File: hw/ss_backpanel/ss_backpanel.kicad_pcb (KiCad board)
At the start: 2 copper layers, 165 x 51.1 mm, 16 parts, among them J101 4mm_banana_socket-LB_I4R_A-pa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, M101 Amphenol_T3437000-DIN7_panel_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, M102 Amphenol_T3437000-DIN7_panel_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, M103 Schurter-3101_0060-fuse_holde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, M104 FN283-1-06_Schaffner_AC-panel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, M105 74980104400-Wurth_RJ45-Panel_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, M106 TE-1734346-Panel_cutout, M107 CUI-UJ2_AH_1_SMT-Panel_cutout, M108 DSub9-Kycon_K22X-E9P-N-panel_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, M109 SJ-3571N_CUI_audio_jacket_pan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

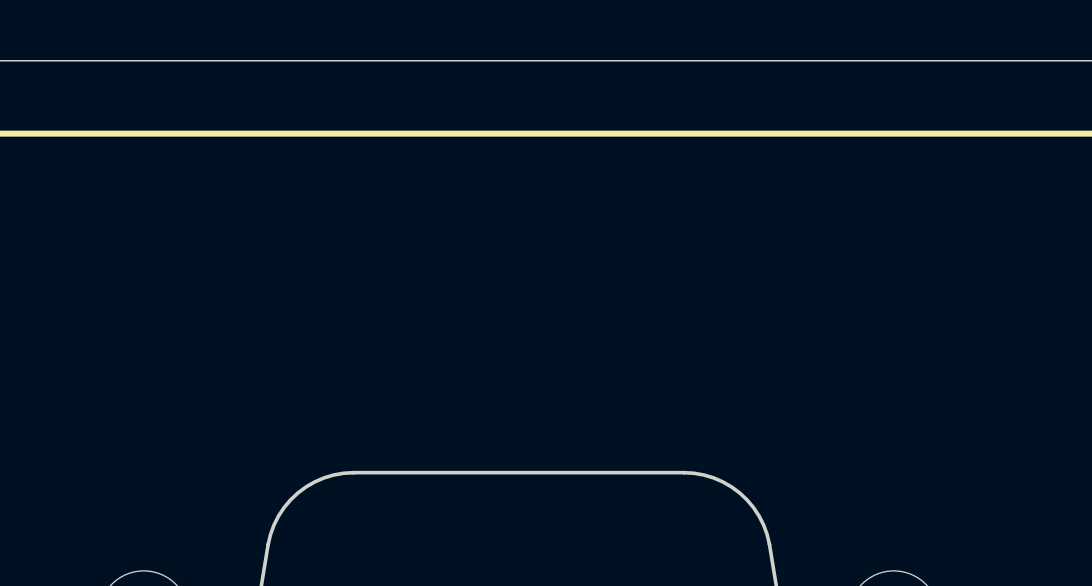
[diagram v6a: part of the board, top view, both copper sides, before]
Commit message: Add 12V DC-out (Molex Nano-Fit 1x02) and SMA in back-panel, for FM antenna & ext. ant.amp. Updated Dsub9 conn to correct component & placement on MB.
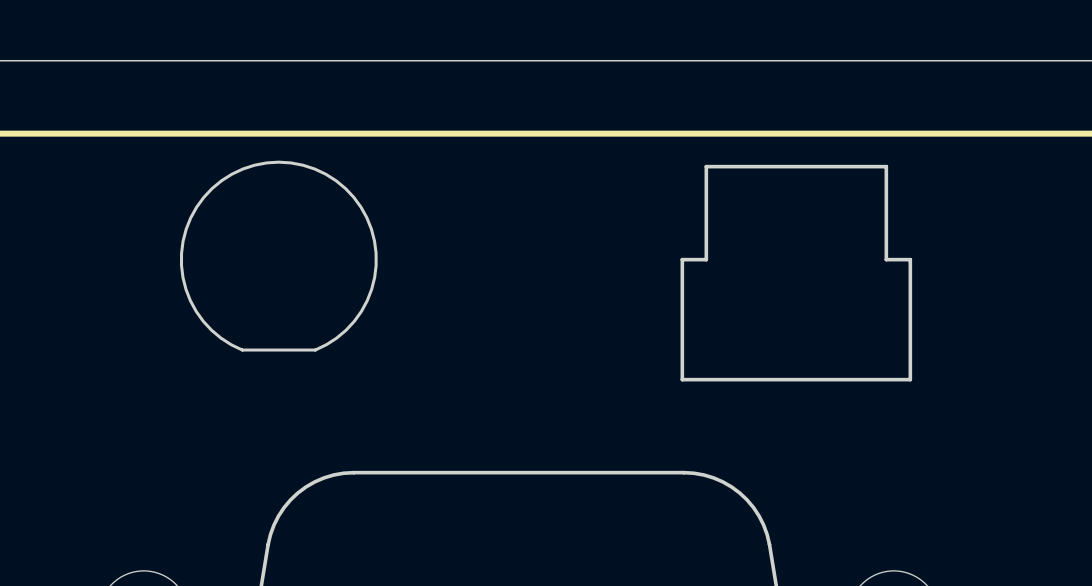
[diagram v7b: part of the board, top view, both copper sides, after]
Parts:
- added M110: SMA_bulkhead_jack_Panel_cutout, customlib_mj_fp:SMA_Bulkhead_jack-Panel_cutout, B.Cu at (95.5, 55.5)
- added M111: Molex_NanoFit-1x02-Panel_cutout, customlib_mj_fp:Molex_NanoFit-1x02-Panel_cutout, B.Cu at (112.8, 59.5)

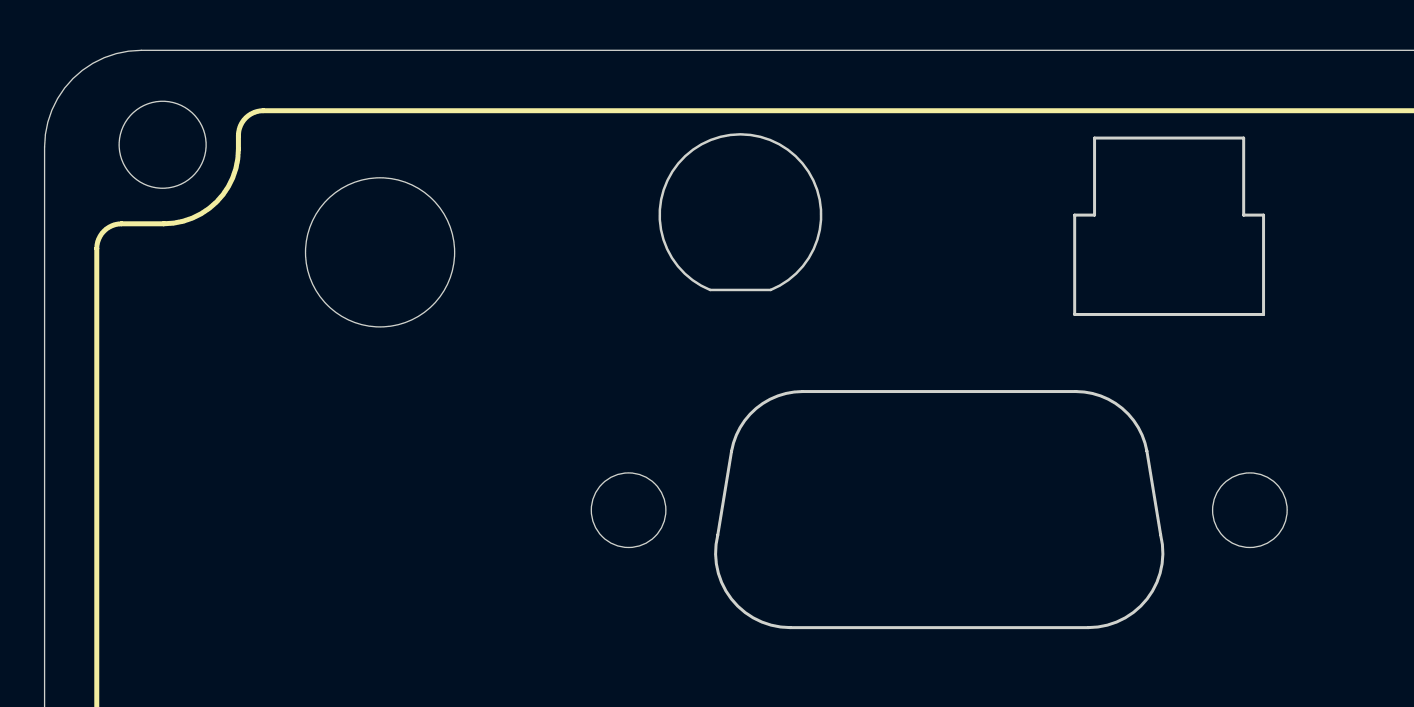
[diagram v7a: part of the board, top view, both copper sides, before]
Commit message: Backpanel: move SMA to side, under MB PCB, also 12V-out moved outwards (and had to shift 12V/Gnd pins);   Mainboard: Move SMA-RA to bottomside, wont fit on Topside. ALso prelim. scatter/placement of some comps.
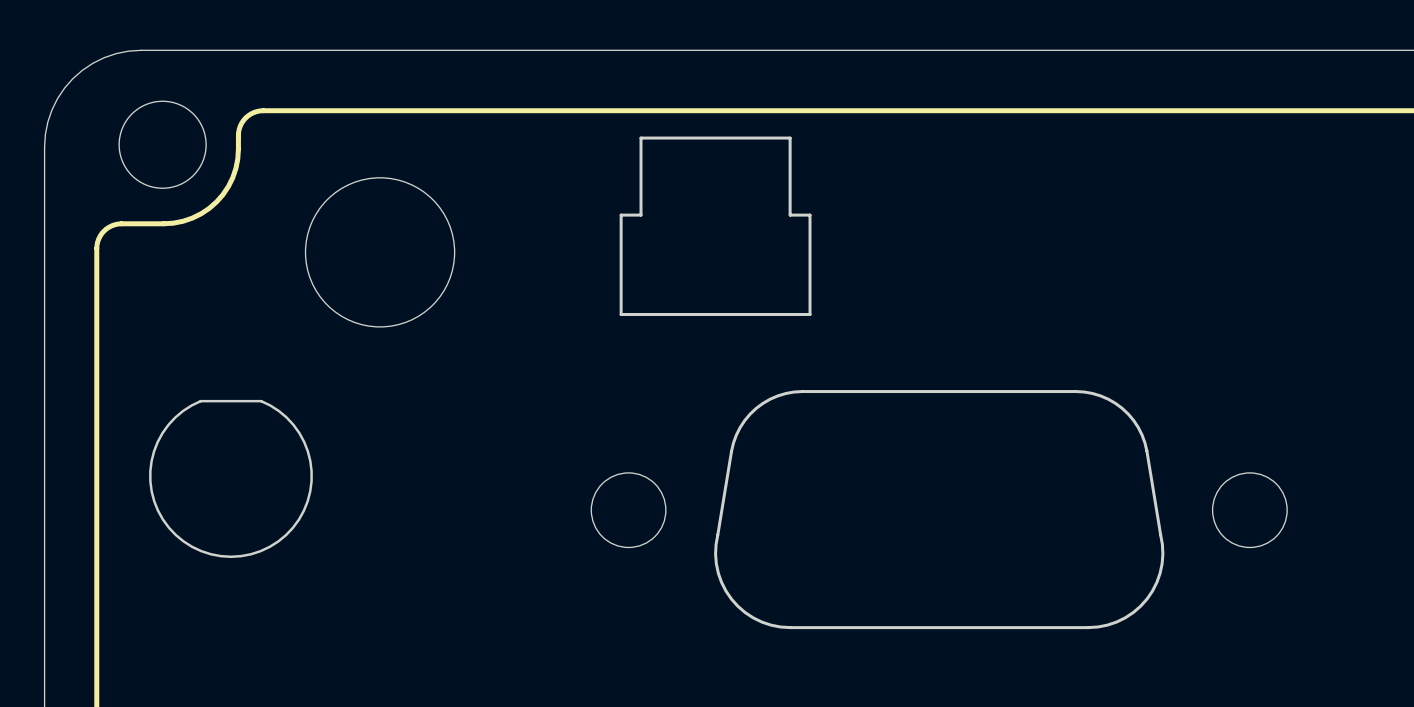
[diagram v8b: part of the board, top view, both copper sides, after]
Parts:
- moved M110 23.0 mm to (75.0, 66.0), turned to 90 degrees
- moved M111 18.2 mm to (94.5, 59.5)
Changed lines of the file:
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@@
     (uvia_drill 0.1)
   )
-  (module customlib_mj_fp:Molex_NanoFit-1x02-Panel_cutout (layer B.Cu)
-    (at 112.75 59.5 180)
+  (module customlib_mj_fp:Molex_NanoFit-1x02-Panel_cutout locked (layer B.Cu)
+    (at 94.5 59.5 180)
     (descr "Panel cut-out for Molex Nano-Fit 1x02")
     (tags "Molex NanoFit panel cut-out")
@@
       (effects (font (size 1 1) (thickness 0.15)) (justify mirror))
     )
+    (fp_line (start -8.910887 7.274234) (end -8.355942 3.89642) (layer Edge.Cuts) (width 0.12))
+    (fp_line (start 6 11) (end -6 11) (layer Edge.Cuts) (width 0.12))
+    (fp_line (start 8.355942 3.89642) (end 8.910887 7.274234) (layer Edge.Cuts) (width 0.12))
+    (fp_line (start -5.5 1.5) (end 5.5 1.5) (layer Edge.Cuts) (width 0.12))
+    (fp_line (start -8.910887 7.274234) (end -8.355942 3.89642) (layer Dwgs.User) (width 0.12))
+    (fp_line (start 6 11) (end -6 11) (layer Dwgs.User) (width 0.12))
+    (fp_line (start 8.355942 3.89642) (end 8.910887 7.274234) (layer Dwgs.User) (width 0.12))
+    (fp_line (start -5.5 1.5) (end 5.5 1.5) (layer Dwgs.User) (width 0.12))
     (fp_arc (start -5.5 4.4) (end -8.355942 3.89642) (angle 80) (layer Dwgs.User) (width 0.12))
     (fp_arc (start 6 8) (end 8.910887 7.274234) (angle 104) (layer Dwgs.User) (width 0.12))
@@
     (fp_arc (start 6 8) (end 8.910887 7.274234) (angle 104) (layer Edge.Cuts) (width 0.12))
     (fp_arc (start -6 8) (end -6 11) (angle 104) (layer Edge.Cuts) (width 0.12))
-    (fp_line (start -8.910887 7.274234) (end -8.355942 3.89642) (layer Edge.Cuts) (width 0.12))
-    (fp_line (start 6 11) (end -6 11) (layer Edge.Cuts) (width 0.12))
-    (fp_line (start 8.355942 3.89642) (end 8.910887 7.274234) (layer Edge.Cuts) (width 0.12))
-    (fp_line (start -5.5 1.5) (end 5.5 1.5) (layer Edge.Cuts) (width 0.12))
-    (fp_line (start -8.910887 7.274234) (end -8.355942 3.89642) (layer Dwgs.User) (width 0.12))
-    (fp_line (start 6 11) (end -6 11) (layer Dwgs.User) (width 0.12))
-    (fp_line (start 8.355942 3.89642) (end 8.910887 7.274234) (layer Dwgs.User) (width 0.12))
-    (fp_line (start -5.5 1.5) (end 5.5 1.5) (layer Dwgs.User) (width 0.12))
     (pad "" np_thru_hole circle (at 12.5 6.275) (size 3 3) (drill 3) (layers *.Cu *.Mask))
     (pad "" np_thru_hole circle (at -12.5 6.275) (size 3 3) (drill 3) (layers *.Cu *.Mask))
@@
   )
   (module customlib_mj_fp:SMA_Bulkhead_jack-Panel_cutout (layer B.Cu)
-    (at 95.5 55.5 270)
+    (at 75 66 90)
     (descr "SMA bulkhead jack connector cut-out")
     (tags "SMA panel cutout")
